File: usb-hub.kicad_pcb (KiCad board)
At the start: 4 copper layers, 23 x 28.1 mm, 51 parts, among them J1 USB_C_Receptacle_16pin, J2 USB_C_Receptacle_16pin, J3 USB_C_Receptacle_16pin, J4 Conn_01x01_Female, J5 Conn_01x01_Female, J6 Conn_01x01_Female, J7 Conn_01x01_Female, Q1 PMOS, -3.6A, 0.02R, Q2 Q_NMOS_GSD 1Amp, SW1 SW_Push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

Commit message: fix mixup of swclk and swdio pads in schematic, updated changed inductor text to board file
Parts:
- L1, L2: value 470R at 100M, 1A -> inductor 470R at 100M, 1A
- R3, R4: value 4.7k, 125mW, 5% -> 2.7k, 125mW, 5%
- moved J4 8.17 mm to (146.2, 95.6)
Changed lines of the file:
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@@
   )
   (layers
-    (0 F.Cu signal)
-    (1 In1.Cu power)
-    (2 In2.Cu power)
+    (0 F.Cu signal hide)
+    (1 In1.Cu power hide)
+    (2 In2.Cu power hide)
     (31 B.Cu signal)
     (32 B.Adhes user hide)
@@
     (at 141.98 97.24)
     (attr smd)
-    (fp_text reference SW1 (at 3.181 -0.593) (layer B.SilkS)
+    (fp_text reference SW1 (at 3.07 -0.65) (layer B.SilkS)
       (effects (font (size 0.7 0.7) (thickness 0.1)) (justify mirror))
     )
@@
       (effects (font (size 0.7 0.7) (thickness 0.1)))
     )
-    (fp_text value "470R at 100M, 1A" (at 0 1.5 180) (layer F.Fab) hide
+    (fp_text value "inductor 470R at 100M, 1A" (at 0 1.5 180) (layer F.Fab) hide
       (effects (font (size 1 1) (thickness 0.15)))
     )
@@
       (effects (font (size 0.7 0.7) (thickness 0.1)) (justify mirror))
     )
-    (fp_text value "470R at 100M, 1A" (at 0 -1.5 202) (layer B.Fab) hide
+    (fp_text value "inductor 470R at 100M, 1A" (at 0 -1.5 202) (layer B.Fab) hide
       (effects (font (size 1 1) (thickness 0.15)) (justify mirror))
     )
@@
       (effects (font (size 0.8 0.8) (thickness 0.1)) (justify mirror))
     )
-    (fp_text value "4.7k, 125mW, 5%" (at 0 -1.5 338) (layer B.Fab) hide
+    (fp_text value "2.7k, 125mW, 5%" (at 0 -1.5 338) (layer B.Fab) hide
       (effects (font (size 1 1) (thickness 0.15)) (justify mirror))
     )
@@
       (effects (font (size 0.7 0.7) (thickness 0.1)) (justify mirror))
     )
-    (fp_text value "4.7k, 125mW, 5%" (at 0 -1.5 338) (layer B.Fab) hide
+    (fp_text value "2.7k, 125mW, 5%" (at 0 -1.5 338) (layer B.Fab) hide
       (effects (font (size 1 1) (thickness 0.15)) (justify mirror))
     )
@@
   )
   (module raise_fp:Fiducial_0.5mm_Dia_1mm_Outer (layer B.Cu)
-    (at 138.575 92.575)
+    (at 146.15 95.64)
     (descr "Circular Fiducial, 0.5mm bare copper top; 1mm keepout (Level C)")
     (tags marker)
@@
     (effects (font (size 1 1) (thickness 0.25)))
   )
-  (gr_text HUB_PCB1 (at 141.986 92.71) (layer B.SilkS)
+  (gr_text HUB_PCB1 (at 141.77 94.09) (layer B.SilkS)
     (effects (font (size 0.7 0.7) (thickness 0.1)) (justify mirror))
   )
-  (gr_text $ver$ (at 141.57 100.92) (layer B.SilkS)
-    (effects (font (size 0.7 0.7) (thickness 0.1)) (justify mirror))
+  (gr_text $ver$ (at 142.01 92.62) (layer B.SilkS)
+    (effects (font (size 0.6 0.5) (thickness 0.1)) (justify mirror))
   )
   (gr_text "d+ d- cc" (at 142.06 99.78) (layer B.SilkS)

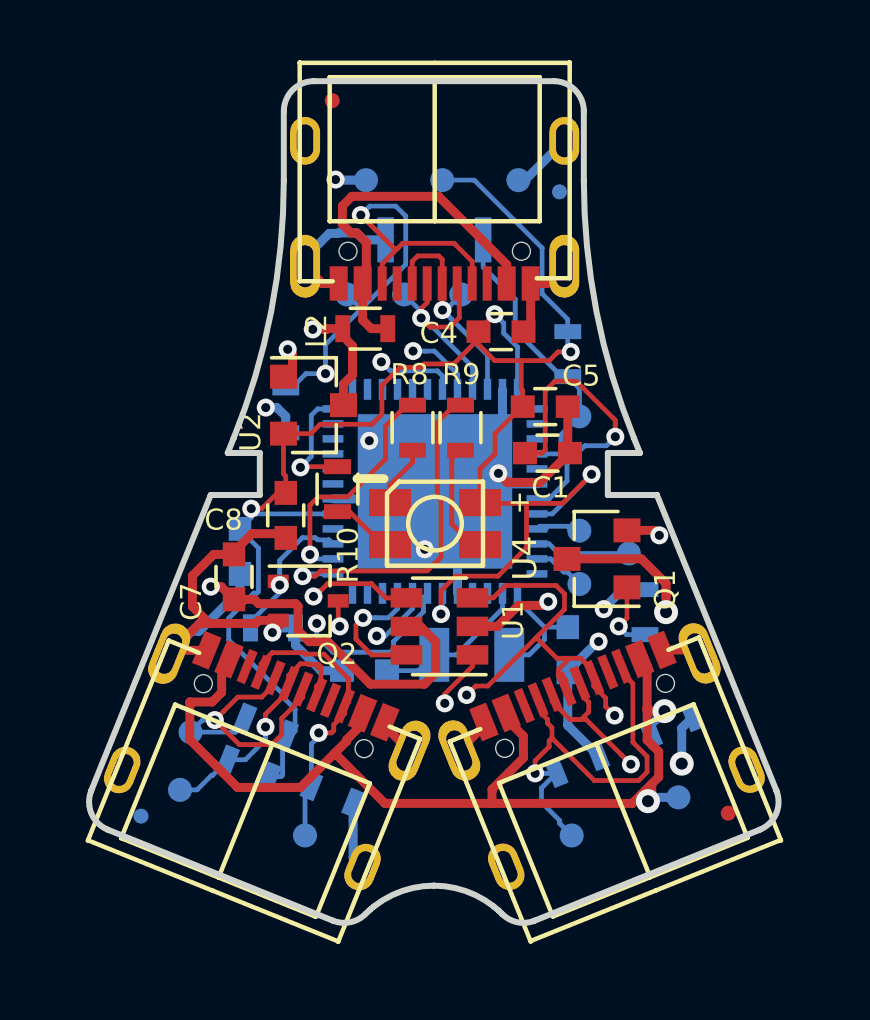
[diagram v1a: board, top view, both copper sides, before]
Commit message: 100pf caps for ESD and I2C level shifter
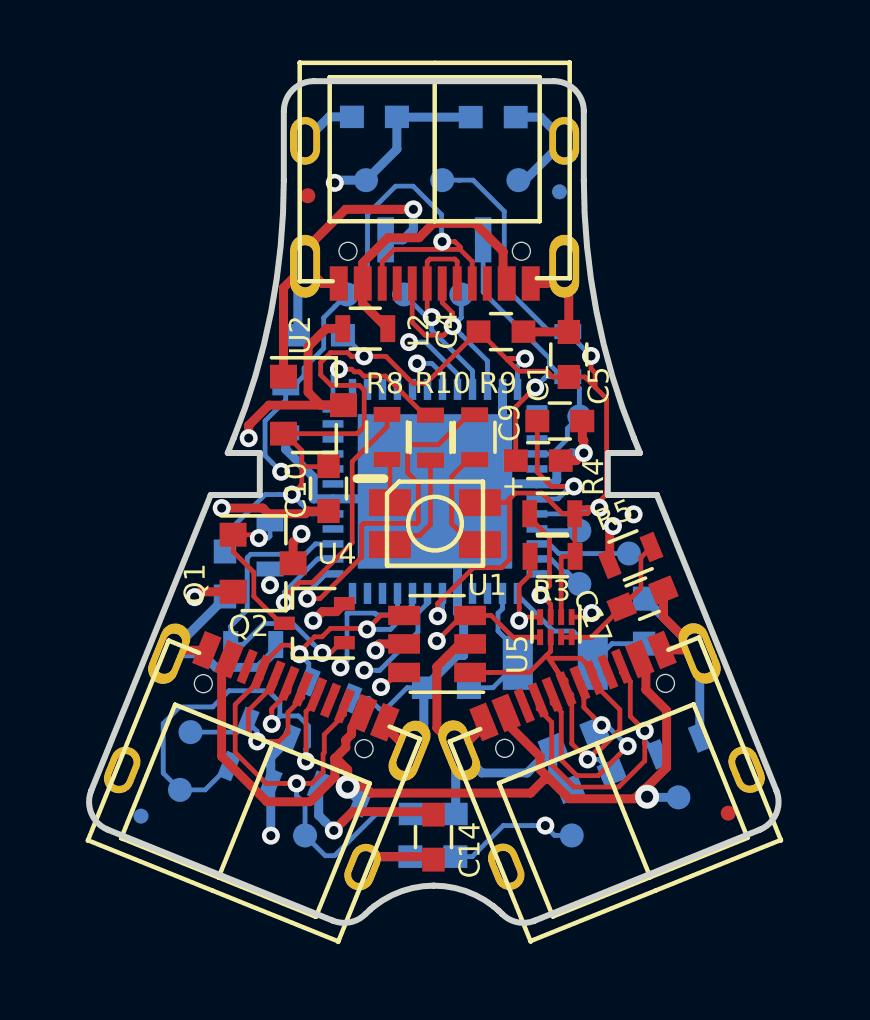
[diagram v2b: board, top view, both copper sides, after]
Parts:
- added C10: 100pF ceramic, 100v, 10%, raise_fp:C_0603, F.Cu at (138.4, 105.5)
- added C11: 100pF ceramic, 100v, 10%, raise_fp:C_0603, B.Cu at (146.6, 113.9)
- added C12: 100pF ceramic, 100v, 10%, raise_fp:C_0603, B.Cu at (147.2, 115.3)
- added C13: 100pF ceramic, 100v, 10%, raise_fp:C_0603, B.Cu at (140.0, 93.1)
- added C14: 100pF ceramic, 100v, 10%, raise_fp:C_0603, F.Cu at (141.9, 117.2)
- added C15: 100pF ceramic, 100v, 10%, raise_fp:C_0603, B.Cu at (141.9, 117.8)
- added C16: 100pF ceramic, 100v, 10%, raise_fp:C_0603, B.Cu at (141.9, 116.4)
- added C17: 100pF ceramic, 100v, 10%, raise_fp:C_0603, F.Cu at (148.9, 109.2)
- added C9: 100pF ceramic, 100v, 10%, raise_fp:C_0603, F.Cu at (145.4, 104.6)
- added R13: 2.7k, 125mW, 5%, raise_fp:R_0603, B.Cu at (136.4, 113.6)
- added R14: 2.7k, 125mW, 5%, raise_fp:R_0603, B.Cu at (135.8, 115.1)
- added R5: 200k, 125mW, 5%, raise_fp:R_0603, F.Cu at (148.5, 107.8)
- added U5: pca9306, Housings_SON:X2SON-8_1.4x1mm_Pitch0.35mm, F.Cu at (146.0, 110.2)
- C7, C8: moved to B.Cu
- R11, R12: value 1M, 125mW, 5% -> 200k, 125mW, 5%
- R3, R4: moved to F.Cu
- moved C7 17.6 mm to (143.9, 93.2), turned to 0 degrees
- moved R4 13.2 mm to (145.9, 106.4), turned to 0 degrees
- moved R1 12.7 mm to (136.5, 107.5), turned to 90 degrees
- moved L1 11.3 mm to (138.8, 115.7), turned to 338 degrees
- moved Q1 11.1 mm to (136.3, 108.0), turned to 0 degrees
- moved R3 11.1 mm to (145.9, 107.8), turned to 0 degrees
- moved C8 6.12 mm to (138.2, 100.4), turned to 180 degrees
- moved R10 3.55 mm to (141.8, 103.8)
- moved R12 3.49 mm to (138.5, 112.2)
- moved R11 3.44 mm to (150.1, 114.1)
- moved J5 3.27 mm to (137.8, 95.8)
- moved Y1 2.80 mm to (146.0, 111.3)
- moved C3 2.79 mm to (142.4, 112.2)
- moved C2 2.72 mm to (149.0, 110.0), turned to 270 degrees
- moved C5 1.91 mm to (146.5, 101.1), turned to 90 degrees
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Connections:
- net Net-(L1-Pad1) renamed /side-power-pre-ferrite
- R3 pad 1: /sda -> /sda33
- R4 pad 1: /scl -> /scl33
- U1 pad 1: /sda -> /scl
- U1 pad 3: /scl -> /sda
- U3 pad 31: /sda -> /sda33
- U3 pad 32: /scl -> /scl33
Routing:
- net Earth: track 73.7 -> 109.8 mm, vias 8 -> 6
- net +5V: track 56.3 -> 80.2 mm, vias 5 -> 7
- net Net-(Q1-Pad1): track 29.0 -> 5.81 mm, vias 2 -> 1
- net /scl33: track 0.00 -> 17.0 mm, vias 0 -> 2
- net /sda33: track 0.00 -> 14.5 mm, vias 0 -> 2
- net /ufp-cc: track 31.2 -> 39.5 mm
- net /side-power-pre-ferrite: track 12.2 -> 19.2 mm
- net /dfp-r-cc: track 29.7 -> 36.6 mm, vias 2 -> 4
- net /sda: track 57.3 -> 50.5 mm
- net /side-switch: track 4.97 -> 10.8 mm
- net Net-(C1-Pad2): track 10.0 -> 4.53 mm
- net Net-(C17-Pad2): track 0.00 -> 4.85 mm
- net /reset: track 9.83 -> 13.4 mm, vias 0 -> 1
- net Net-(J1-PadA4/B9): track 12.4 -> 9.27 mm
- net /side-power: track 34.4 -> 31.6 mm
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
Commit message: split git version into git and date
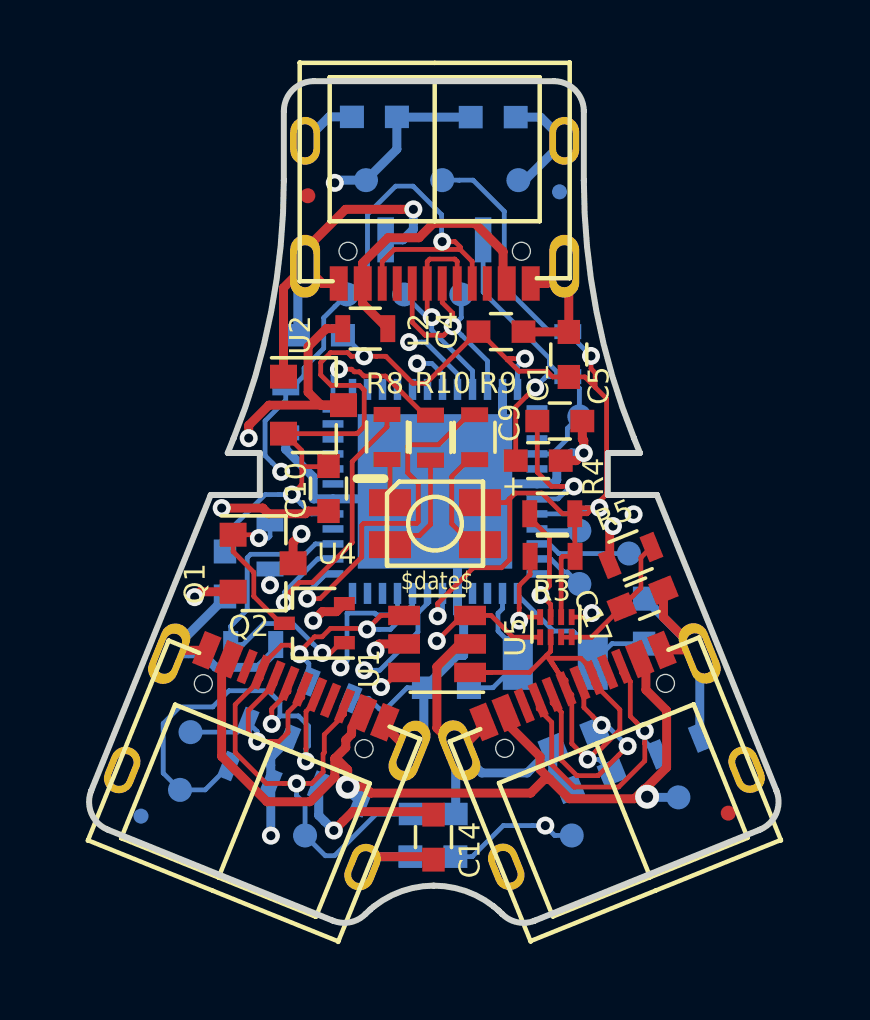
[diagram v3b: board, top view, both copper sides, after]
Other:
- board text added: "$date$"
- board text added: "$git$"
- board text removed: "$ver$"
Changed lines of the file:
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@@
   (general
     (thickness 0.8)
-    (drawings 116)
+    (drawings 117)
     (tracks 833)
     (zones 0)
@@
   )
   (layers
-    (0 F.Cu signal)
-    (1 In1.Cu power)
-    (2 In2.Cu power)
-    (31 B.Cu signal)
+    (0 F.Cu signal hide)
+    (1 In1.Cu power hide)
+    (2 In2.Cu power hide)
+    (31 B.Cu signal hide)
     (32 B.Adhes user hide)
     (33 F.Adhes user hide)
@@
     (pad_to_mask_clearance 0.2)
     (aux_axis_origin 0 0)
-    (visible_elements FFFDBF7F)
+    (visible_elements FFFCBF7F)
     (pcbplotparams
       (layerselection 0x00008_7ffffff8)
@@
     (tags SOT-23-6)
     (attr smd)
-    (fp_text reference U1 (at -1.67 1.96) (layer F.SilkS)
+    (fp_text reference U1 (at 2.26 -0.82 90) (layer F.SilkS)
       (effects (font (size 0.7 0.7) (thickness 0.1)))
     )
@@
     (tags "X2SON-8 1.4x1mm Pitch0.35mm")
     (attr smd)
-    (fp_text reference U5 (at 0.91 1.28 90) (layer F.SilkS)
+    (fp_text reference U5 (at 0.33 1.35 90) (layer F.SilkS)
       (effects (font (size 0.7 0.7) (thickness 0.1)))
     )
@@
       (rotate (xyz 0 0 0))
     )
+  )
+  (gr_text $date$ (at 142.07 108.61) (layer F.SilkS)
+    (effects (font (size 0.6 0.5) (thickness 0.1)))
   )
   (gr_line (start 138.98 101.04) (end 138.98 102.04) (layer Dwgs.User) (width 0.2))
@@
     (effects (font (size 0.7 0.7) (thickness 0.1)) (justify mirror))
   )
-  (gr_text $ver$ (at 140.7 110.44) (layer B.SilkS)
+  (gr_text $git$ (at 140.7 110.44) (layer B.SilkS)
     (effects (font (size 0.6 0.5) (thickness 0.1)) (justify mirror))
   )

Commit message: changed visible layers, removed drawings
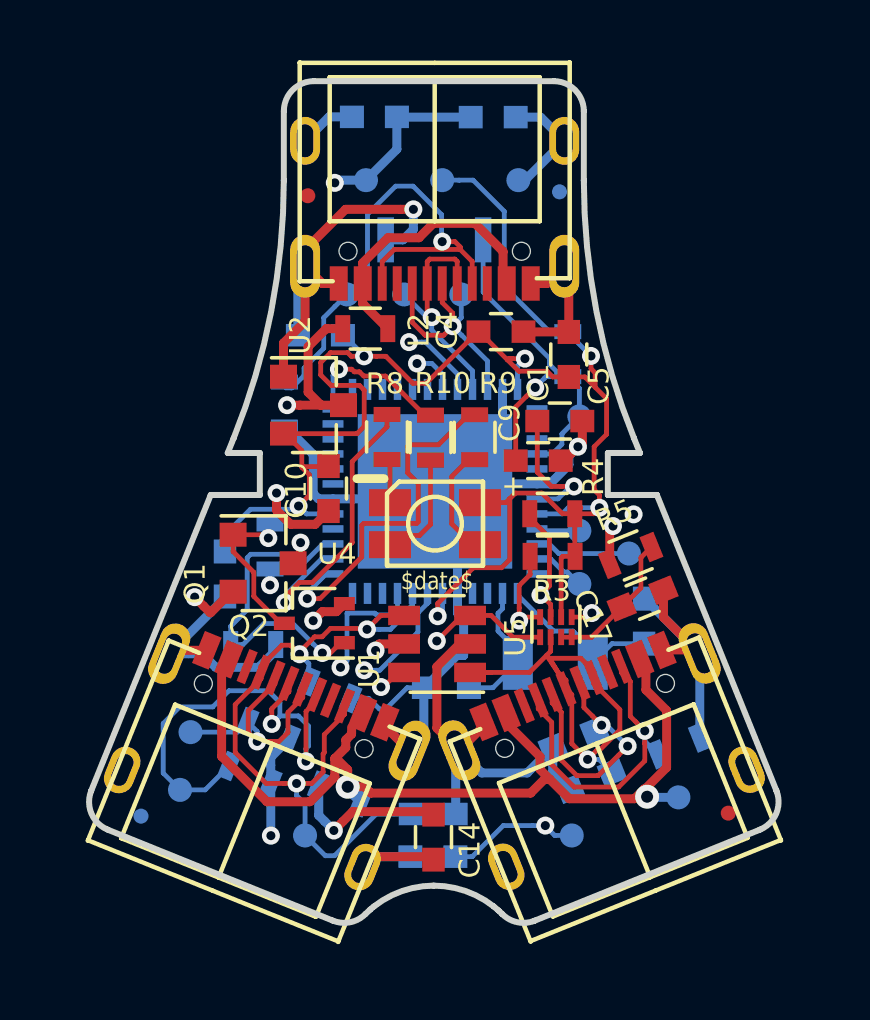
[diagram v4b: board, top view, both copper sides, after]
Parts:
- moved R6 0.20 mm to (137.0, 102.7)
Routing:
- net +5V: track 80.2 -> 76.5 mm
- net /ufp-cc: track 39.5 -> 36.2 mm, vias 3 -> 2
- net Earth: track 109.8 -> 108.3 mm

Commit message: slight change to USBC routing and changed USBC connectors mask around locator pins
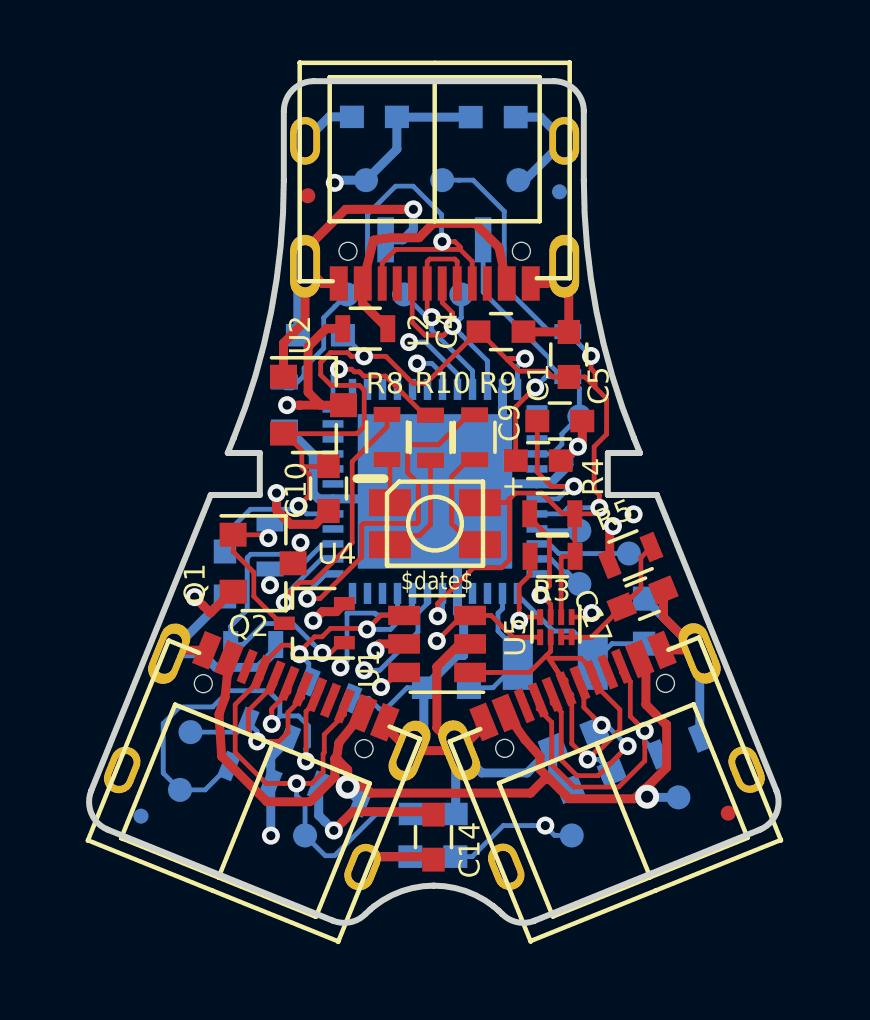
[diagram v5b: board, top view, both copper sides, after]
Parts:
- J2: footprint raise_fp:usb-c-16smt -> usb-c-16smt
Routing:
- net Earth: track 108.3 -> 110.0 mm
- net /side-power: track 31.6 -> 32.6 mm

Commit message: increased outline of edge cuts
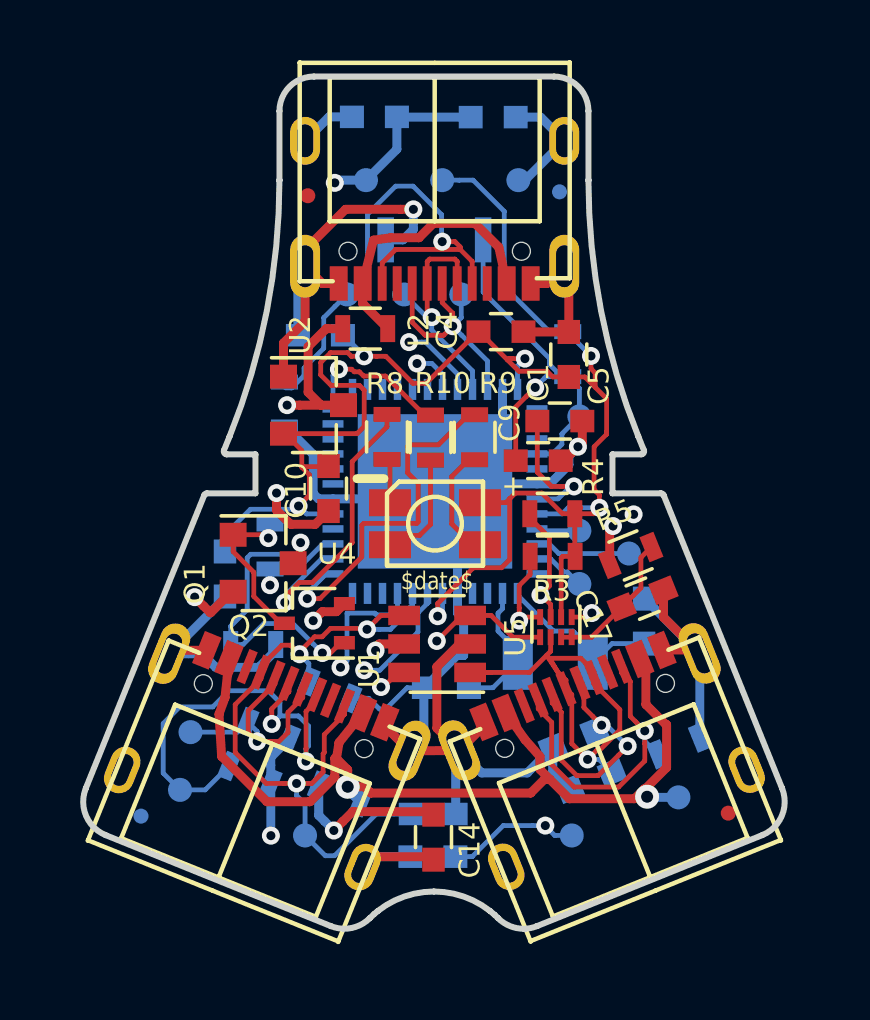
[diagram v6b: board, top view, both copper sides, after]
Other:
- board size 23 x 28.1 mm -> 23.4 x 28.4 mm

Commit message: added big pads for USBC
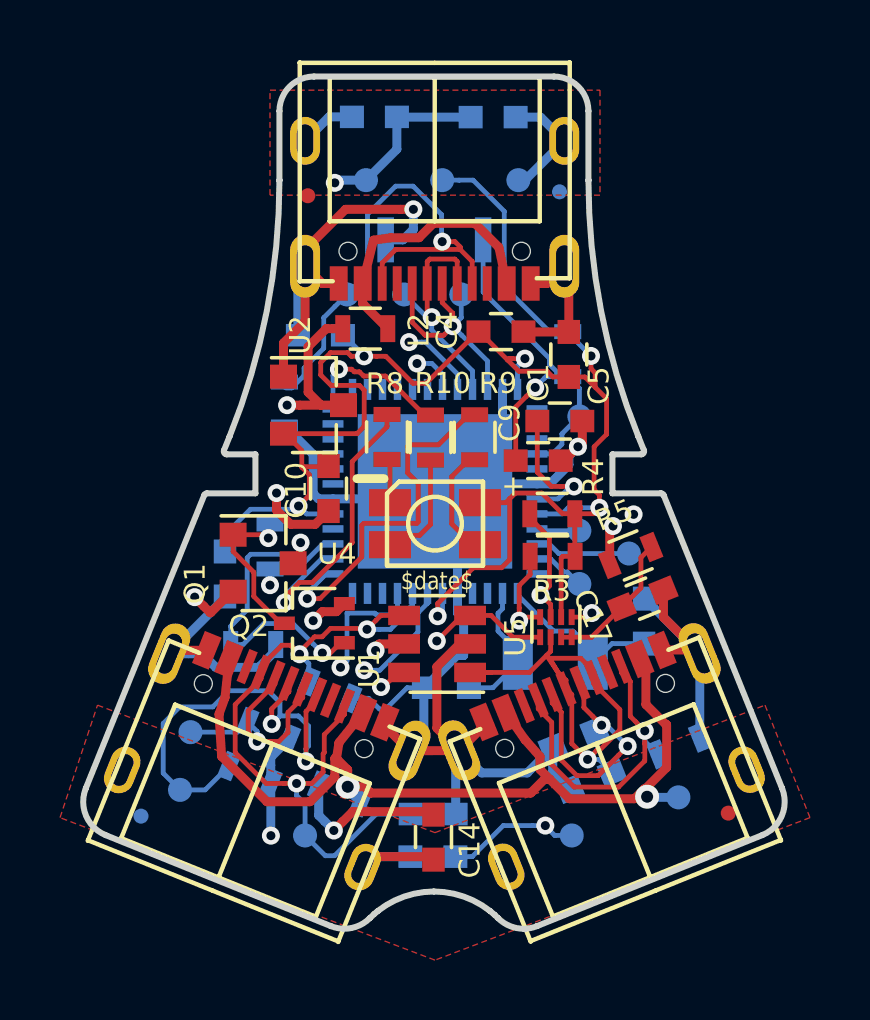
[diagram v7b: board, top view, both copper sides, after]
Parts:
- J2: footprint usb-c-16smt -> raise_fp:usb-c-16smt
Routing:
- added copper zone on F.Cu, net Earth
